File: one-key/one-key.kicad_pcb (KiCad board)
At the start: 2 copper layers, 14.4 x 14.4 mm, 8 parts, among them J1 USB_OTG, J2 Conn_01x04, SW1 SW_Push, U1 C8051F38x_32

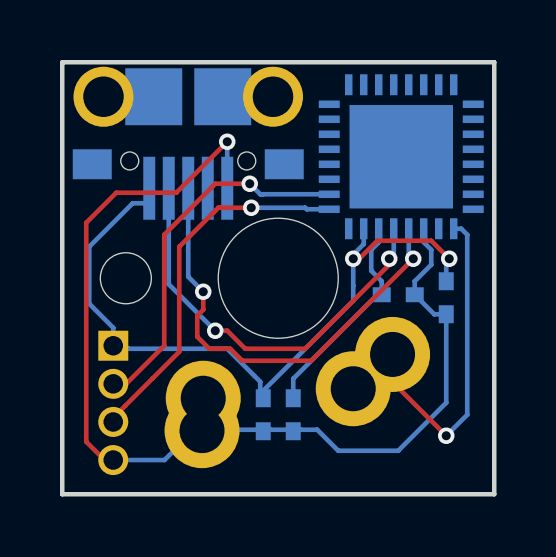
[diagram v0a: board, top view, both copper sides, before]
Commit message: vbus sense pin needs to be connected
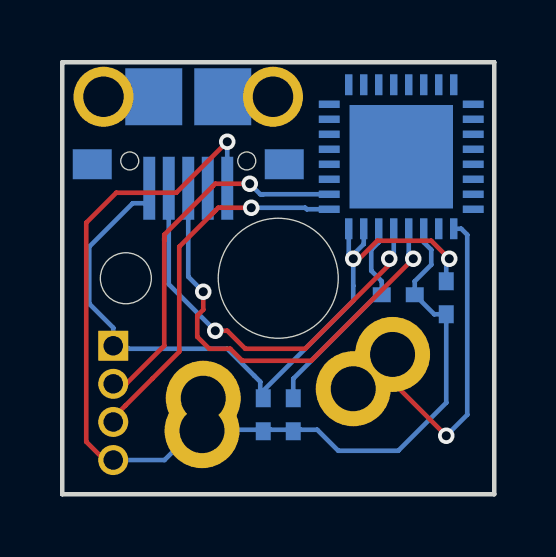
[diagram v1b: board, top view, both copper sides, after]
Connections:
- U1 pad 8: Net-(U1-Pad8) -> +5V
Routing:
- net +5V: track 24.9 -> 26.0 mm

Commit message: add images and license text
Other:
- rule pad_to_mask_clearance: 0.2 -> 0.03
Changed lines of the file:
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@@
     (pad_size 2 2)
     (pad_drill 1.35)
-    (pad_to_mask_clearance 0.2)
+    (pad_to_mask_clearance 0.03)
     (aux_axis_origin 0 0)
     (visible_elements FFFFFF3F)
@@
   (segment (start 158 101.04) (end 158 101) (width 0.155) (layer F.Cu) (net 8))
   (segment (start 158 101.04) (end 158.06 101.04) (width 0.155) (layer B.Cu) (net 8) (status 30))
-  (segment (start 165.85 94.6) (end 165.85 95.45) (width 0.155) (layer B.Cu) (net 16) (status 400000))
+  (segment (start 165.85 94.6) (end 165.85 95.45) (width 0.155) (layer B.Cu) (net 16))
   (segment (start 165.85 95.45) (end 166 95.6) (width 0.155) (layer B.Cu) (net 16))
   (segment (start 166 95.6) (end 166 95.46159) (width 0.155) (layer B.Cu) (net 16))
